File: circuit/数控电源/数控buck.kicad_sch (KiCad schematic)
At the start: 78 parts, among them J1 Conn_01x06_MountingPin, J2 Conn_01x02, J4 Conn_01x04_MountingPin, J5 Conn_01x02, Q1 BSC070N10NS3G, Q2 BSC070N10NS3G, SW1 SW_Push, U1 STM32F334R8Tx, U2 LM5164DDA, U3 LM1117DT-3.3, U4 LM5109MA, U5 INA240A1PW, U6 TLV9062, U8 LM2675M-5, Y1 Crystal_GND24

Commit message: 配置了dac和comp和hrtim定时器
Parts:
- D2: value SS34 -> SS26
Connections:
- net +3.3V: now also R9.2
- net NRST: now also C11.2, R9.1, SW1.2; no longer R9.2
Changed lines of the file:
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@@
 	(wire
 		(pts
+			(xy 149.86 30.48) (xy 142.24 30.48)
+		)
+		(stroke
+			(width 0)
+			(type default)
+		)
+	)
+	(wire
+		(pts
 			(xy 344.17 80.01) (xy 346.71 80.01)
 		)
@@
 		)
 	)
-	(label "NRST"
-		(at 142.24 19.05 180)
-		(effects
-			(font
-				(size 1.27 1.27)
-			)
-			(justify right bottom)
-		)
-	)
 	(label "USART3_TX"
 		(at 25.4 71.12 180)
@@
 		)
 	)
+	(label "NRST"
+		(at 149.86 30.48 180)
+		(effects
+			(font
+				(size 1.27 1.27)
+			)
+			(justify right bottom)
+		)
+	)
 	(label "U1_RX"
 		(at 115.57 62.23 180)
@@
 			)
 		)
-		(property "Value" "SS34"
+		(property "Value" "SS26"
 			(at 68.8975 209.55 0)
 			(effects
@@
 					(unit 1)
 				)
+			)
+		)
+	)
+	(symbol
+		(lib_id "power:+3.3V")
+		(at 142.24 19.05 0)
+		(unit 1)
+		(exclude_from_sim no)
+		(in_bom yes)
+		(on_board yes)
+		(dnp no)
+		(fields_autoplaced yes)
+		(property "Reference" "#PWR059"
+			(at 142.24 22.86 0)
+			(effects
+				(font
+					(size 1.27 1.27)
+				)
+				(hide yes)
+			)
+		)
+		(property "Value" "+3.3V"
+			(at 142.24 13.97 0)
+			(effects
+				(font
+					(size 1.27 1.27)
+				)
+			)
+		)
+		(property "Footprint" ""
+			(at 142.24 19.05 0)
+			(effects
+				(font
+					(size 1.27 1.27)
+				)
+				(hide yes)
+			)
+		)
+		(property "Datasheet" ""
+			(at 142.24 19.05 0)
+			(effects
+				(font
+					(size 1.27 1.27)
+				)
+				(hide yes)
+			)
+		)
+		(property "Description" "Power symbol creates a global label with name \"+3.3V\""
+			(at 142.24 19.05 0)
+			(effects
+				(font
+					(size 1.27 1.27)
+				)
+				(hide yes)
+			)
+		)
+		(pin "1"
+		)
+		(instances
+			(project "数控buck"
+				(path "/80f4f4fe-c3fa-41cd-a010-dacb4b3084d3"
+					(reference "#PWR059")
+					(unit 1)
+				)

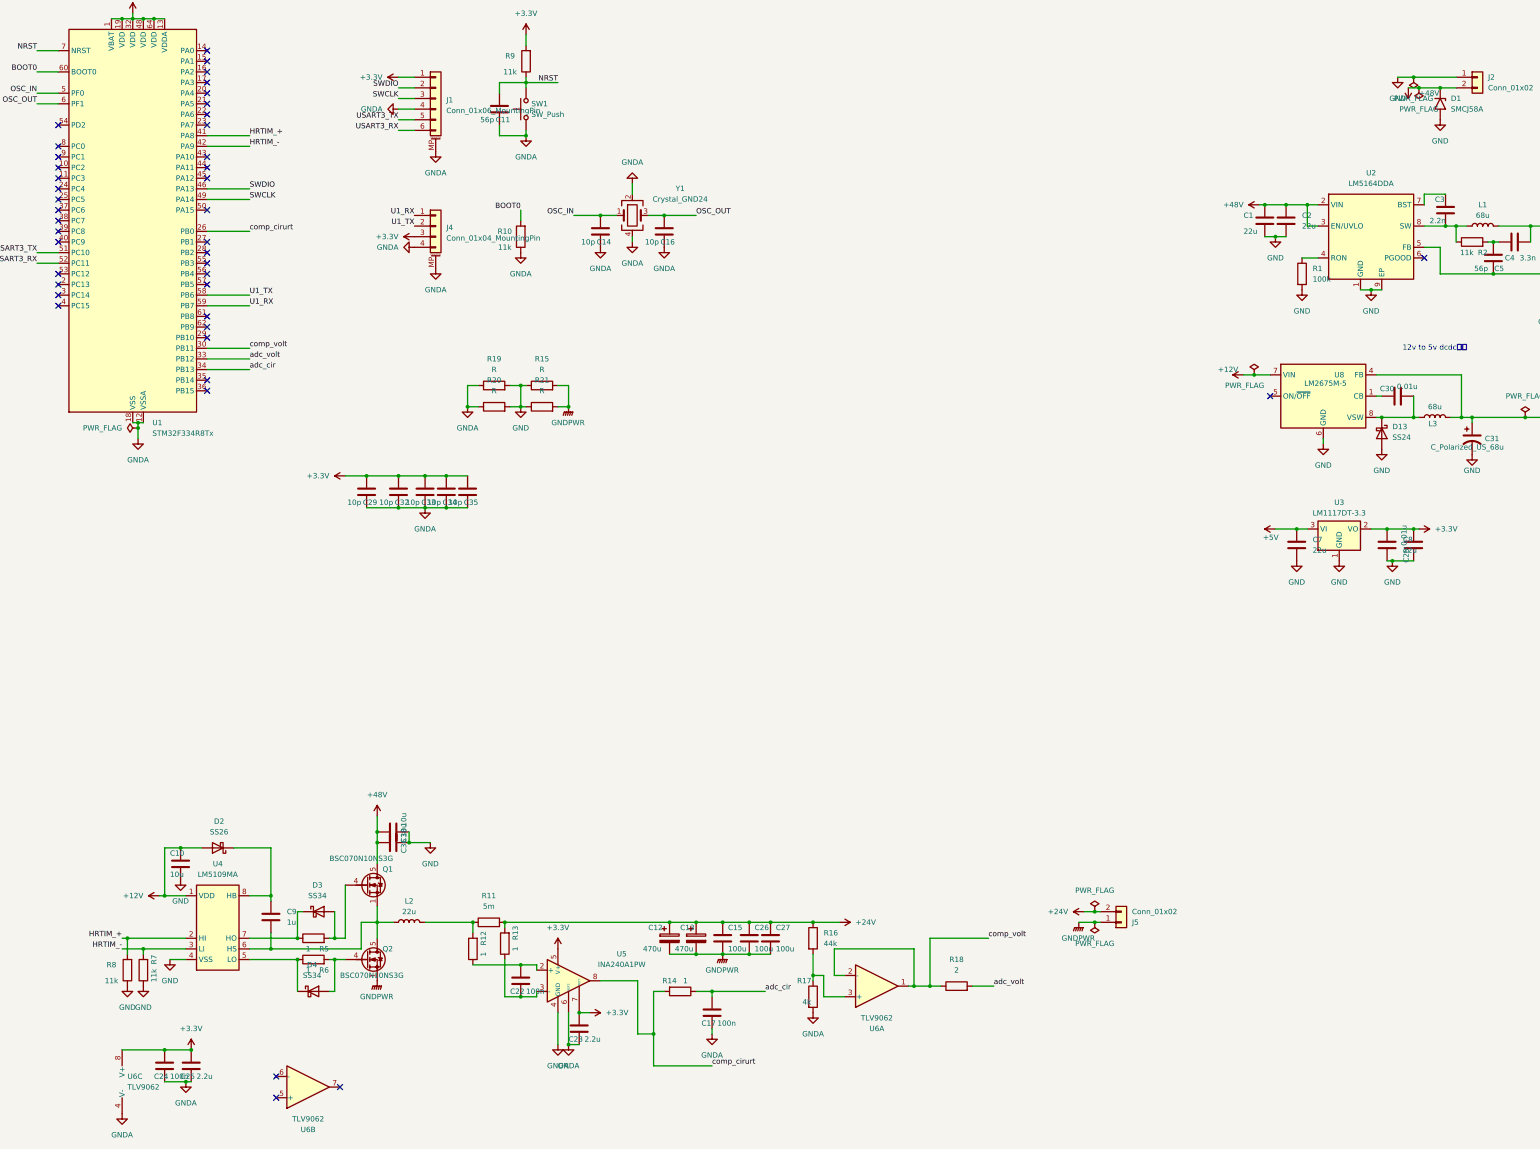
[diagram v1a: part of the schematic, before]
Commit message: recover second board layout
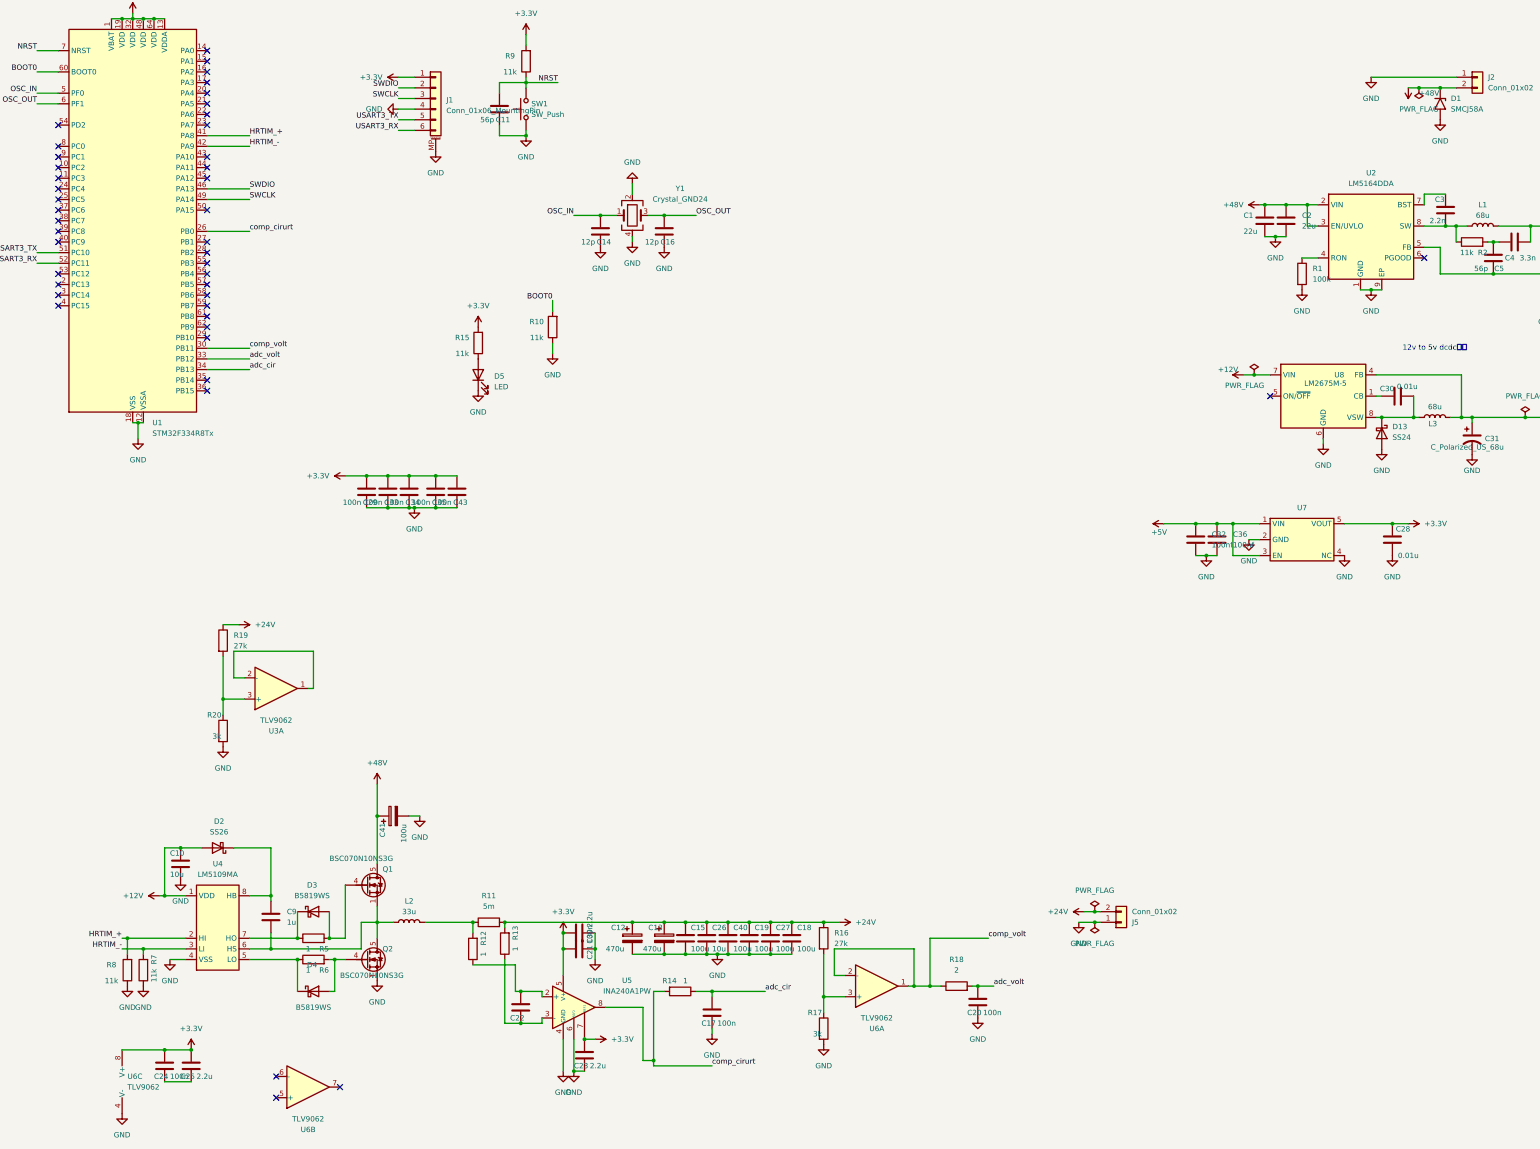
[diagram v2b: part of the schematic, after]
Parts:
- removed C38: 10u, Capacitor_SMD:C_1206_3216Metric, symbol Device:C
- removed C7, C8: 22u, Capacitor_SMD:C_0805_2012Metric_Pad1.18x1.45mm_HandSolder, symbol Device:C
- removed D3, D4: SS34, Diode_SMD:D_SMA, symbol Diode:SS34
- removed J4: Conn_01x04_MountingPin, Connector_JST:JST_GH_SM04B-GHS-TB_1x04-1MP_P1.25mm_Horizontal, symbol Connector_Generic_MountingPin:Conn_01x04_MountingPin
- removed R21: R, Resistor_SMD:R_0805_2012Metric_Pad1.20x1.40mm_HandSolder, symbol Device:R
- removed U3: LM1117DT-3.3, Package_TO_SOT_SMD:TO-252-3_TabPin2, symbol Regulator_Linear:LM1117DT-3.3
- added C18, C19, C40: 100u, Capacitor_SMD:C_0805_2012Metric_Pad1.18x1.45mm_HandSolder, symbol Device:C
- added C20, C21, C43: 100n, Capacitor_SMD:C_0603_1608Metric, symbol Device:C
- added C39: 2.2u, Capacitor_SMD:C_0603_1608Metric, symbol Device:C
- added C41: 100u, Capacitor_SMD:CP_Elec_10x10.5, symbol Device:C_Polarized
- added D3, D4: B5819WS, Diode_SMD:D_SOD-323, symbol Diode:BAT48JFILM
- added D5: LED, LED_SMD:LED_0603_1608Metric_Pad1.05x0.95mm_HandSolder, symbol Device:LED
- added U3: TLV9062, Package_SO:SOIC-8_3.9x4.9mm_P1.27mm, symbol Amplifier_Operational:TLV9062
- added U7: ~, Package_TO_SOT_SMD:SOT-23-5, symbol Regulator_Linear:RT9013
- C14, C16: value 10p -> 12p
- C26: value 100u -> 10u
- C29, C33, C34, C35: value 10p -> 100n
- C32: value 10p -> 100nf
- C36: value 10u -> 100nf; footprint Capacitor_SMD:C_1206_3216Metric -> Capacitor_SMD:C_0603_1608Metric
- D1: footprint Diode_SMD:D_SMB -> Diode_SMD:D_SOD-123F
- L2: value 22u -> 33u
- R15: value R -> 11k; footprint Resistor_SMD:R_0805_2012Metric_Pad1.20x1.40mm_HandSolder -> Resistor_SMD:R_0603_1608Metric_Pad0.98x0.95mm_HandSolder
- R16: value 44k -> 27k
- R17: value 4k -> 3k
- R19: value R -> 27k; footprint Resistor_SMD:R_0805_2012Metric_Pad1.20x1.40mm_HandSolder -> Resistor_SMD:R_0603_1608Metric_Pad0.98x0.95mm_HandSolder
- R20: value R -> 3k; footprint Resistor_SMD:R_0805_2012Metric_Pad1.20x1.40mm_HandSolder -> Resistor_SMD:R_0603_1608Metric_Pad0.98x0.95mm_HandSolder
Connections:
- net +24V: now also R19.1, C18.1, C19.1, C40.1
- net +3.3V: now also R15.2, C21.2, C39.2, C43.2, U7.5 (VOUT); no longer C32.2
- net +48V: now also C41.1; no longer C36.2
- net +5V: now also C32.1, C36.1, U7.1 (VIN), U7.3 (EN)
- net GND: now also C11.1, C12.2, C13.2, C14.1, C15.2, C16.1, C17.1, C23.1, C26.2, C27.2, C29.1, C32.2, C33.1, C34.1, C35.1, C36.2, J1.4 (Pin_4), J1.MP (MountPin), J5.1 (Pin_1), Q2.1 (S), Q2.2 (S), Q2.3 (S), R10.1, R17.2, SW1.1, U1.12 (VSSA), U1.18 (VSS), U1.31 (VSS), U1.47 (VSS), U1.63 (VSS), U5.1 (GND), U5.4 (GND), U5.6 (REF2), U6.4 (V-), Y1.2, Y1.4, C18.2, C19.2, C20.1, C21.1, C39.1, C40.2, C41.2, C43.1, D5.1 (K), U7.2 (GND), U7.4 (NC); no longer C36.1, R15.1, R19.2
- net adc_volt: now also C20.2
- net at R6.1, U4.5 (LO): now also D4.1 (K)
- net at R5.1, U4.7 (HO): now also D3.1 (K)
- net at Q1.4 (G), R5.2: now also D3.2 (A)
- net at Q2.4 (G), R6.2: now also D4.2 (A)
- removed net GNDA: C11.1, C14.1, C16.1, C17.1, C23.1, C24.1, C25.1, C29.1, C32.1, C33.1, C34.1, C35.1, J1.4 (Pin_4), J1.MP (MountPin), R10.1, R17.2, R19.1, R20.1, SW1.1, U1.12 (VSSA), U1.18 (VSS), U1.31 (VSS), U1.47 (VSS), U1.63 (VSS), U5.1 (GND), U5.4 (GND), U5.6 (REF2), U6.4 (V-), Y1.2, Y1.4
- removed net GNDPWR: C12.2, C13.2, C15.2, C26.2, C27.2, J5.1 (Pin_1), Q2.1 (S), Q2.2 (S), Q2.3 (S), R15.2
- net U1_RX: no longer names the net of U1.59 (PB7)
- net U1_TX: no longer names the net of U1.58 (PB6)
- new net: R19.2, R20.1, U3.3 (+)
- new net: D5.2 (A), R15.1
- new net: C24.1, C25.1
- new net: U3.1, U3.2 (-)
- no-connect marks 42 -> 44
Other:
- moved on the sheet: C12, C13, C15, C22, C23, C26, C28, R10, R16, R17, U5

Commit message: 完成第二版电路版布局
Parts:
- removed C17, C20: 100n, Capacitor_SMD:C_0603_1608Metric, symbol Device:C
- removed C23, C39: 2.2u, Capacitor_SMD:C_0603_1608Metric, symbol Device:C
- removed C41: 100u, Capacitor_SMD:CP_Elec_10x10.5, symbol Device:C_Polarized
- added C38, C7: 10u, Capacitor_SMD:C_1210_3225Metric, symbol Device:C
- added C8: 10u, Capacitor_SMD:C_1210_3225Metric_Pad1.33x2.70mm_HandSolder, symbol Device:C
- added unit 2 of U3
- added unit 3 of U3
- R11: footprint Resistor_SMD:R_2512_6332Metric_Pad1.40x3.35mm_HandSolder -> Resistor_SMD:R_1206_3216Metric_Pad1.30x1.75mm_HandSolder
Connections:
- net +24V: no longer R19.1
- net +3.3V: now also U3.8 (V+)
- net +48V: now also R19.1, C38.2, C7.2, C8.2
- net GND: now also C38.1, C7.1, C8.1, U3.4 (V-)
- net adc_Vin: now reaches U1.35 (PB14)
- net adc_Vin: now also U3.1, U3.2 (-)
- no-connect marks 44 -> 46
